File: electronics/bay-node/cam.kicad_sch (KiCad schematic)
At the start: 13 parts, among them J6 CAM, Q4 AO3400A, U12 USBLC6-2SC6, U13 USBLC6-2SC6

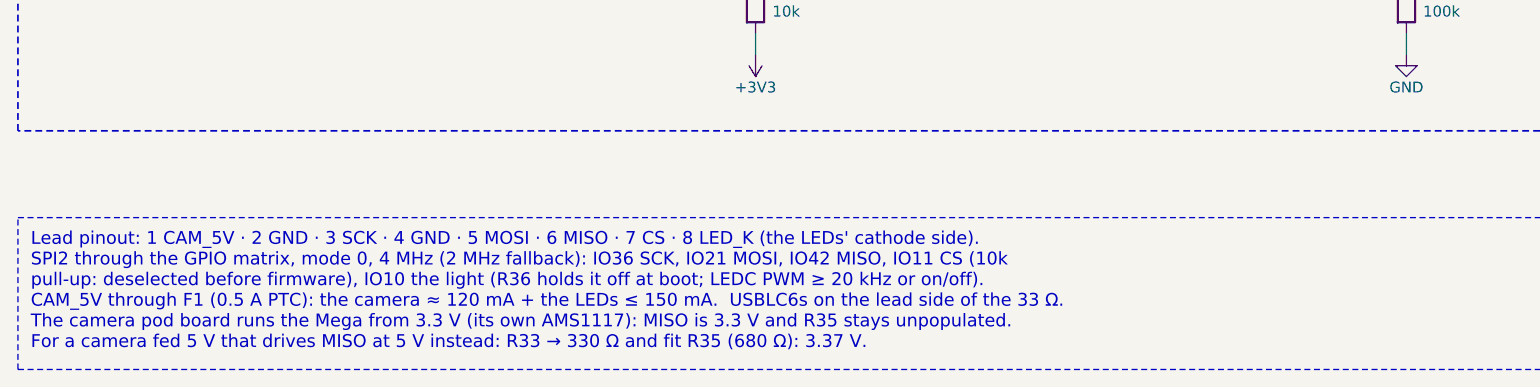
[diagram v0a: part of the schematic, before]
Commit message: PCBA review: hub and node fixes before the order
On main's CH224A hub and the bay node v0.5.

Power hub:
- CPL: the side LEDs (C598310, C4555382) +0.825 mm, their polarity
  proven from JLC's own footprints (and C495809 at 270 deg in the table,
  for the IRF7842 the AP33772S hub had).
- Rows: SHDN pull-downs 10k, so rows stay off without firmware (100k
  gave 1 V at the pin's 10 uA); a B5819W at each row output for the
  cable's kick; the red FAULT LEDs fed from their ROW_EN, so a row that
  is simply off shows no fault.
- In2's VRACK band 8 mm wide; the console's USB pair hand-routed on
  F.Cu over In1 (U5's channels in the pair's order), EN's capacitor at
  the module's pin; reliefs on both pads of C2, C10, R3, C11-C14; notes
  corrected, the outputs sheet on A2.
- The PESD2CAN kept and documented (no stocked CAN TVS stays off at
  29.4 V and clamps under +40 V).

Bay node:
- SW3 placed on its pegs (-0.55 mm, Shouhan's land pattern); 2.2k I2C
  pull-ups; POS_IN 470k; AUX_VREF 1k; 100k on SVC; U9's input on a +5V
  island with three vias, C20 at its pins; C12 relieved; the camera note
  and the catalog's MPN text corrected.

Both re-routed: ERC 0, DRC 0 (the known C8 silkscreen warning), parity
0; CPL audit against JLC's footprints: every part agrees but SW3's pads
(0.13 mm, on purpose).  Bring-up measurements in assembly.md, the
resolution in pcba-review.md.

Co-Authored-By: Claude Opus 5.5 <noreply@anthropic.com>
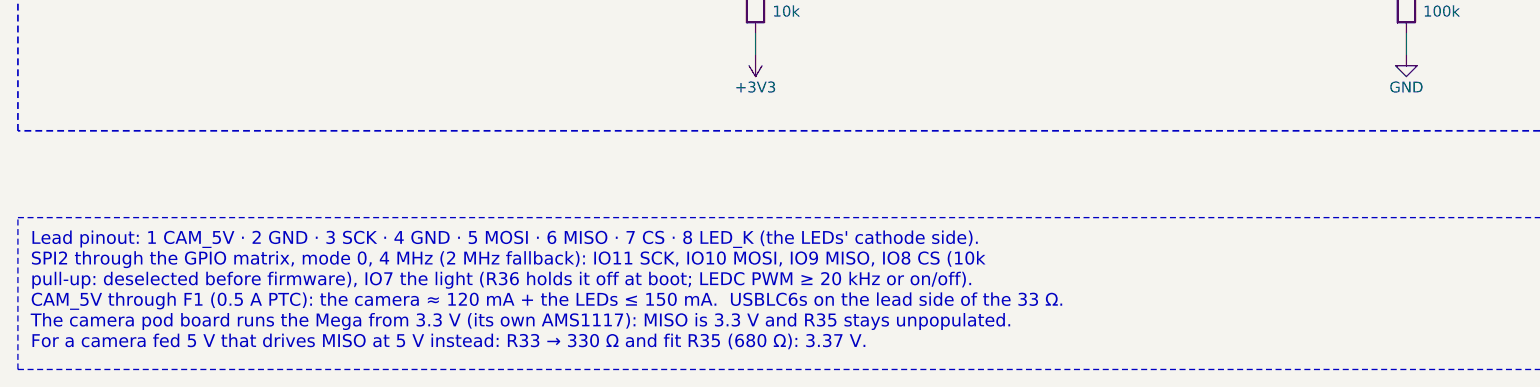
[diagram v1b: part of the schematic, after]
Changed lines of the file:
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@@
 		)
 	)
-	(text_box "Lead pinout: 1 CAM_5V · 2 GND · 3 SCK · 4 GND · 5 MOSI · 6 MISO · 7 CS · 8 LED_K (the LEDs' cathode side).\nSPI2 through the GPIO matrix, mode 0, 4 MHz (2 MHz fallback): IO36 SCK, IO21 MOSI, IO42 MISO, IO11 CS (10k\n  pull-up: deselected before firmware), IO10 the light (R36 holds it off at boot; LEDC PWM ≥ 20 kHz or on/off).\nCAM_5V through F1 (0.5 A PTC): the camera ≈ 120 mA + the LEDs ≤ 150 mA.  USBLC6s on the lead side of the 33 Ω.\nThe camera pod board runs the Mega from 3.3 V (its own AMS1117): MISO is 3.3 V and R35 stays unpopulated.\n  For a camera fed 5 V that drives MISO at 5 V instead: R33 → 330 Ω and fit R35 (680 Ω): 3.37 V."
+	(text_box "Lead pinout: 1 CAM_5V · 2 GND · 3 SCK · 4 GND · 5 MOSI · 6 MISO · 7 CS · 8 LED_K (the LEDs' cathode side).\nSPI2 through the GPIO matrix, mode 0, 4 MHz (2 MHz fallback): IO11 SCK, IO10 MOSI, IO9 MISO, IO8 CS (10k\n  pull-up: deselected before firmware), IO7 the light (R36 holds it off at boot; LEDC PWM ≥ 20 kHz or on/off).\nCAM_5V through F1 (0.5 A PTC): the camera ≈ 120 mA + the LEDs ≤ 150 mA.  USBLC6s on the lead side of the 33 Ω.\nThe camera pod board runs the Mega from 3.3 V (its own AMS1117): MISO is 3.3 V and R35 stays unpopulated.\n  For a camera fed 5 V that drives MISO at 5 V instead: R33 → 330 Ω and fit R35 (680 Ω): 3.37 V."
 		(exclude_from_sim no)
 		(at 15.24 162.56 0)

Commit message: Bay node: AP2114H for the 3.3 V, camera ESD clamped to +3V3
The schematic counter-review's fixes, approved by the user.

- U2: AP2114H-3.3TRG1 (C150716, catalog ldo_1a) instead of the AMS1117-3.3.
  It is specified stable with ceramics (C11, C12); the AMS1117 guarantees it
  only with 22 uF tantalum.  Same SOT-223 "H" pinout (1 GND, 2 and tab VOUT,
  3 VIN), footprint and copper: only the part's properties change.
- U12, U13 (USBLC6 on the camera lead): pin 5 on +3V3 instead of CAM_5V.
  With CAM_5V off (the PTC tripped), the SPI lines would feed the pod through
  the upper diodes, and CAM_5V's clamp sits above the ESP32's 3.6 V.  A
  minimal patch of the routing, no re-route: the CAM_5V stub that only
  reached the two pins goes (10 segments); U12.5 gets a +3V3 feed to a via in
  In2's +3V3 area; U13.5, with no room for its own, joins U12.5 along the
  stub's old east path at 0.25 mm.  The straightening pass ran on +3V3 and
  CAM_5V.
- Stale notes: AUX_VREF goes through R23's 1k, not 33 ohms; the next node's
  pull-down is R29's 470k, not 100k.
- pcbgen.fanout_pads takes `only` (REF.PAD), to fan out a few pads of a
  routed board.

ERC 0, DRC 0, unconnected 0, parity 0, every 3D model found.  The renders,
Gerbers and viewer model are regenerated (the unchanged iso render kept).
The schematic, the BOM and the docs (the node table, the CPL fix table, the
bring-up check, PCBA review N9) follow.  The hub and bom/ are untouched.

Co-Authored-By: Claude Opus 5.5 <noreply@anthropic.com>
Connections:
- net +3V3: now also U12.5 (VBUS), U13.5 (VBUS)
- net CAM_5V: no longer U12.5 (VBUS), U13.5 (VBUS)
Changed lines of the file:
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@@
 		)
 	)
-	(label "CAM_5V"
-		(at 193.04 48.26 90)
-		(fields_autoplaced yes)
-		(effects
-			(font
-				(size 1.27 1.27)
-			)
-			(justify left bottom)
+	(symbol
+		(lib_id "power:+3V3")
+		(at 193.04 48.26 0)
+		(unit 1)
+		(exclude_from_sim no)
+		(in_bom yes)
+		(on_board yes)
+		(dnp no)
+		(fields_autoplaced yes)
+		(property "Reference" "#PWR07006"
+			(at 193.04 48.26 0)
+			(effects
+				(font
+					(size 1.27 1.27)
+				)
+				(hide yes)
+			)
+		)
+		(property "Value" "+3V3"
+			(at 193.04 44.45 0)
+			(effects
+				(font
+					(size 1.27 1.27)
+				)
+			)
+		)
+		(property "Footprint" ""
+			(at 193.04 48.26 0)
+			(effects
+				(font
+					(size 1.27 1.27)
+				)
+				(hide yes)
+			)
+		)
+		(property "Datasheet" ""
+			(at 193.04 48.26 0)
+			(effects
+				(font
+					(size 1.27 1.27)
+				)
+				(hide yes)
+			)
+		)
+		(property "Description" ""
+			(at 193.04 48.26 0)
+			(effects
+				(font
+					(size 1.27 1.27)
+				)
+				(hide yes)
+			)
+		)
+		(pin "1"
+		)
+		(instances
+			(project "bay-node"
+				(path "/76847c0c-2f76-566c-8109-428b2bf58b3f/12078ac0-2350-591d-80c3-fc5243dd3b60"
+					(reference "#PWR07006")
+					(unit 1)
+				)
+			)
 		)
 	)
@@
 		(dnp no)
 		(fields_autoplaced yes)
-		(property "Reference" "#PWR07006"
+		(property "Reference" "#PWR07007"
 			(at 193.04 106.68 0)
 			(effects
@@
 			(project "bay-node"
 				(path "/76847c0c-2f76-566c-8109-428b2bf58b3f/12078ac0-2350-591d-80c3-fc5243dd3b60"
-					(reference "#PWR07006")
+					(reference "#PWR07007")
 					(unit 1)
 				)
@@
 		)
 	)
-	(label "CAM_5V"
-		(at 193.04 88.9 90)
-		(fields_autoplaced yes)
-		(effects
-			(font
-				(size 1.27 1.27)
-			)
-			(justify left bottom)
+	(symbol
+		(lib_id "power:+3V3")
+		(at 193.04 88.9 0)
+		(unit 1)
+		(exclude_from_sim no)
+		(in_bom yes)
+		(on_board yes)
+		(dnp no)
+		(fields_autoplaced yes)
+		(property "Reference" "#PWR07008"
+			(at 193.04 88.9 0)
+			(effects
+				(font
+					(size 1.27 1.27)
+				)
+				(hide yes)
+			)
+		)
+		(property "Value" "+3V3"
+			(at 193.04 85.09 0)
+			(effects
+				(font
+					(size 1.27 1.27)
+				)
+			)
+		)
+		(property "Footprint" ""
+			(at 193.04 88.9 0)
+			(effects
+				(font
+					(size 1.27 1.27)
+				)
+				(hide yes)
+			)
+		)
+		(property "Datasheet" ""
+			(at 193.04 88.9 0)
+			(effects
+				(font
+					(size 1.27 1.27)
+				)
+				(hide yes)
+			)
+		)
+		(property "Description" ""
+			(at 193.04 88.9 0)
+			(effects
+				(font
+					(size 1.27 1.27)
+				)
+				(hide yes)
+			)
+		)
+		(pin "1"
+		)
+		(instances
+			(project "bay-node"
+				(path "/76847c0c-2f76-566c-8109-428b2bf58b3f/12078ac0-2350-591d-80c3-fc5243dd3b60"
+					(reference "#PWR07008")
+					(unit 1)
+				)
+			)
 		)
 	)
@@
 		(dnp no)
 		(fields_autoplaced yes)
-		(property "Reference" "#PWR07007"
+		(property "Reference" "#PWR07009"
 			(at 205.74 139.7 0)
 			(effects
@@
 			(project "bay-node"
 				(path "/76847c0c-2f76-566c-8109-428b2bf58b3f/12078ac0-2350-591d-80c3-fc5243dd3b60"
-					(reference "#PWR07007")
+					(reference "#PWR07009")
 					(unit 1)
 				)
@@
 		(dnp no)
 		(fields_autoplaced yes)
-		(property "Reference" "#PWR07008"
+		(property "Reference" "#PWR07010"
 			(at 177.8 143.51 0)
 			(effects
@@
 			(project "bay-node"
 				(path "/76847c0c-2f76-566c-8109-428b2bf58b3f/12078ac0-2350-591d-80c3-fc5243dd3b60"
-					(reference "#PWR07008")
+					(reference "#PWR07010")
 					(unit 1)
 				)
@@
 		(dnp no)
 		(fields_autoplaced yes)
-		(property "Reference" "#PWR07009"
+		(property "Reference" "#PWR07011"
 			(at 213.36 78.74 0)
 			(effects
@@
 			(project "bay-node"
 				(path "/76847c0c-2f76-566c-8109-428b2bf58b3f/12078ac0-2350-591d-80c3-fc5243dd3b60"
-					(reference "#PWR07009")
+					(reference "#PWR07011")
 					(unit 1)
 				)

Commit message: Schematic review S1, S4, S6: POS_IN 150k, the hub's ON LEDs on 18k, the camera's 0.75 A PTC
The user approved them ("S1 oui / S6 oui / S4 oui").

* S1, bay node: R29 470k -> 150k (C22807, basic).
  - Before its firmware runs, the upstream POS output (a node's IO42, the
    hub's IO10-13) floats. The BAT54S's warm leakage (about 2-3 uA at
    65 C) could then lift POS_IN through 470k to VIL.
  - Driven high through R30 + R28, 150k still gives 2.87 V, above VIH.
  - The design.py notes and bay_node.dtsi follow.
* S4, power hub: R41-R44 (the ON LEDs on the row outputs) 10k -> 18k
  (C25810, already on the board): 1.4 mA and 37 mW at 28 V. The 10k
  ran at 75 % of its 0603 rating at 29.4 V.
* S6, bay node: F1 (CAM_5V) goes from the 0.5 A PTC to SMD1206P075TF
  (RUILON, C20987, new catalog key pptc750): 0.75 A hold, 1.5 A trip,
  the same 1206 footprint. It is extended like C20799, so no fee changes.
  - Arducam gives the Mega 317 mA working: with the LEDs that is
    ~0.42 A on CAM_5V, where the 0.5 A part holds ~0.31 A at 70 C.
  - The camera pod's LDO tab gets the copper its routing leaves: a
    top-side +3V3 pour round the tab and a bottom-side island, joined by
    three vias. U1 drops ~0.5 W at 317 mA. The routing is unchanged.
  - The "~120 mA" notes go to 317 mA (node and pod design.py,
    electronics.md).
  - The bay's worst case follows: <= 2.25 A on +5V, the buck's inductor
    peaking at ~2.65 A (under its 2.9 A minimum limit), 13.5 W from
    VRACK (power-distribution-review.md, the buck notes).

The routed PCBs keep their routing.
- Node and hub: only the changed parts' properties (KiCad's Python, as
  pcbgen sets them).
- Pod: the two new zones and three vias, refilled.
- ERC 0, DRC 0, unconnected 0, parity 0 on all three (run on the Mac:
  zephyrbox didn't answer).
- keep_unchanged kept the node's renders and the hub's Gerbers. The
  hub's bottom render is restored: 9 pixels of via-hole noise, as before.
- The pod's renders, Gerbers and viewer GLB chang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
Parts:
- F1: value 0.5A -> 0.75A; LCSC C20799 -> C20987; MPN SMD1206P050TF -> SMD1206P075TF
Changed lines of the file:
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@@
 			)
 		)
-		(property "Value" "0.5A"
+		(property "Value" "0.75A"
 			(at 50.8 38.176 90)
 			(effects
@@
 			)
 		)
-		(property "Description" "PTC 0.5 A hold, 1206"
+		(property "Description" "PTC 0.75 A hold, 1.5 A trip, 1206"
 			(at 50.8 35.56 0)
 			(effects
@@
 			)
 		)
-		(property "MPN" "SMD1206P050TF"
+		(property "MPN" "SMD1206P075TF"
 			(at 50.8 35.56 0)
 			(effects
@@
 			)
 		)
-		(property "LCSC" "C20799"
+		(property "LCSC" "C20987"
 			(at 50.8 35.56 0)
 			(effects
@@
 		)
 	)
-	(text_box "Lead pinout: 1 CAM_5V · 2 GND · 3 SCK · 4 GND · 5 MOSI · 6 MISO · 7 CS · 8 LED_K (the LEDs' cathode side).\nSPI2 through the GPIO matrix, mode 0, 4 MHz (2 MHz fallback): IO11 SCK, IO10 MOSI, IO9 MISO, IO8 CS (10k\n  pull-up: deselected before firmware), IO7 the light (R36 holds it off at boot; LEDC PWM ≥ 20 kHz or on/off).\nCAM_5V through F1 (0.5 A PTC): the camera ≈ 120 mA + the LEDs ≤ 150 mA.  USBLC6s on the lead side of the 33 Ω.\nThe camera pod board runs the Mega from 3.3 V (its own AMS1117): MISO is 3.3 V and R35 stays unpopulated.\n  For a camera fed 5 V that drives MISO at 5 V instead: R33 → 330 Ω and fit R35 (680 Ω): 3.37 V."
+	(text_box "Lead pinout: 1 CAM_5V · 2 GND · 3 SCK · 4 GND · 5 MOSI · 6 MISO · 7 CS · 8 LED_K (the LEDs' cathode side).\nSPI2 through the GPIO matrix, mode 0, 4 MHz (2 MHz fallback): IO11 SCK, IO10 MOSI, IO9 MISO, IO8 CS (10k\n  pull-up: deselected before firmware), IO7 the light (R36 holds it off at boot; LEDC PWM ≥ 20 kHz or on/off).\nCAM_5V through F1 (0.75 A PTC, 1.5 A trip): the camera ≤ 317 mA (Arducam) + the LEDs ≤ 102 mA.  USBLC6s on the lead side of the 33 Ω.\nThe camera pod board runs the Mega from 3.3 V (its own AMS1117): MISO is 3.3 V and R35 stays unpopulated.\n  For a camera fed 5 V that drives MISO at 5 V instead: R33 → 330 Ω and fit R35 (680 Ω): 3.37 V."
 		(exclude_from_sim no)
 		(at 15.24 162.56 0)

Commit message: Datasheet audit F1-F6: the pod's AP2114H, STB 5.1k, PC_DET hysteresis, the camera ESD's 100 nF, the eFuse step
The user approved the audit's fixes for the node, the hub and the pod
("Go pour 1"); docs/datasheet-audit.md marks F1-F6 applied.

* F1, camera pod: U1 AMS1117-3.3 -> AP2114H-3.3TRG1 (C150716, catalog
  ldo_1a, the node's U2).
  - The AMS1117 is specified stable only with 22 uF tantalum; the
    AP2114H is stable with the ceramic C2.
  - Same SOT-223 pinout, copper (the +3V3 pour and island round the
    tab stay) and 180 deg CPL correction.
  - One more extended type on the pod's Economic order: +$3.09 and
    $0.05 of parts (JLC_SINCE_QUOTE).
* F2, power hub: R214 (TJA1462 STB pull-down) 10k -> 5.1k (C23186,
  already on the board). With IO9 floating, STB's internal pull-up
  (20 kOhm minimum) left it at up to 1.10 V, over VIL 0.99 V.
* F3, bay node: R42 150k from MUX_SEL back to PC_DET, beside U7 (C22807,
  on the board since S1).
  - The laptop's VBUS rises at ~50 us/V through R11/R12, where the
    LVC1G32 wants <= 10 ns/V and warns of oscillation.
  - This gives ~0.14 V of hysteresis.
* F4, bay node: C28 100 nF (C14663) on U12/U13's VBUS pins (+3V3), above
  U12 by its pin 5. Between the two ICs their courtyards leave no room.
* F5, node and hub: firmware.md's first-flash procedure gains the
  irreversible DIS_USB_OTG_DOWNLOAD_MODE eFuse step. In USB-OTG
  download boot the ROM drives IO40 high: the node's DUT_FLT_N, the
  hub's PD_SCL. Nothing is burnt.
* F6, notes, hub:
  - the IMON filter is 0.9 ms, not 47 us: the pin is a current source;
  - the buck stops at ~3.8 V (internal UVLO);
  - SHDN turns on at >= 1 V;
  - the soft start stays under the limit only typically;
  - the CH224A note follows CH224 V2.1: the source PDOs are listed for
    both parts and readable under 100 W, which is still to check with
    ours (review R3); single-byte transfers; no "same die".
* F6, notes, node: TPS2553D; the LDO's 1.94 V x 0.4 A ~ 0.8 W; L1's
  7.5 A guarante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
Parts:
- added C28: 100n, Capacitor_SMD:C_0603_1608Metric, symbol Device:C
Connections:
- net +3V3: now also C28.1
- net GND: now also C28.2

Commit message: Boards: labelled bottom test pads; hub dVdT 100 nF, 50 ms FLT blank
Eve's DFT rule on the four boards this session owns: bare pads on the
bottom, named on B.SilkS, out of the BOM and the CPL (no part, no
assembly fee).  Supply pads 1.5 mm, signal pads 1.0 mm (new catalog
entry "testpad1"), all more than 2 mm from any THT pad or hole
(closest: 4.7 mm, the pod's TP4).  Positions are fixed in design.py,
so they stay put across revisions.

- bay node, 17: TX, RX, 3V3, GND by the module (kept), then EN, IO0,
  FLT (DUT_FLT_N), ALRT (INA_ALERT_N), SDA, SCL and a second GND;
  a supply row along the bottom edge: GND, VIN, 5V, 3V3, DUT 5V,
  CAM 5V
- power hub, 20: TX, RX, 3V3, GND, 5V, VRACK, GND (kept), then EN,
  IO0, the CH224A's PD SDA/SCL, each row's FLT and IMON (A-D) and a
  third GND in the middle
- camera pod, 4: GND, 5V, 3V3 and a second GND at the far end
- DATA port, 2: GND and 5V (VBUS, through a via under its track)

Hub, as the datasheet audit's U1 answer asks (TPS2660 Fig. 55 at
85 C: 8-10 ms at 21 W fails the 47 nF worst start, 33 ms at 14 W
covers 100 nF): C21-C24 dVdT 47 nF -> 100 nF, so a row's soft start
is 16-22 ms and dissipates about 7-9 W typical, 14 W worst, for
19-24 ms; the firmware's HUB_ROW_FLT_BLANK_MS goes 25 -> 50 ms to
cover it (worst case 39 ms).  docs/power.md, the audit row and the
hub notes say so.

Routing fallout: J1's A12/B1 GND now leaves through one drawn 0.5 mm
via so the automatic fan-out can't cut the VRACK pour off A9/B4; the
pod's LDO tab zones are exclusive so tracks no longer split them.

All four rerouted, tidied and checked: ERC 0, DRC 0, unconnected 0,
parity 0.  Gerbers, renders, schematics, viewer GLBs, the JLC
snapshot lines and the rack BOM regenerated.

Co-Authored-By: Claude Opus 5.5 <noreply@anthropic.com>
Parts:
- added TP10: CAM_5V, TestPoint:TestPoint_Pad_D1.5mm, symbol Connector:TestPoint
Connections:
- net CAM_5V: now also TP10.1
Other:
- note added: "CAM_5V test pad (bottom side, in the supply row)"
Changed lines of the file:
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@@
+		)
+	)
+	(symbol
+		(lib_id "Connector:TestPoint")
+		(at 345.44 35.56 90)
+		(unit 1)
+		(exclude_from_sim no)
+		(in_bom no)
+		(on_board yes)
+		(dnp no)
+		(fields_autoplaced yes)
+		(property "Reference" "TP10"
+			(at 338.276 34.29 90)
+			(effects
+				(font
+					(size 1.27 1.27)
+				)
+			)
+		)
+		(property "Value" "CAM_5V"
+			(at 337.226 36.83 90)
+			(effects
+				(font
+					(size 1.27 1.27)
+				)
+			)
+		)
+		(property "Footprint" "TestPoint:TestPoint_Pad_D1.5mm"
+			(at 345.44 35.56 0)
+			(effects
+				(font
+					(size 1.27 1.27)
+				)
+				(hide yes)
+			)
+		)
+		(property "Datasheet" ""
+			(at 345.44 35.56 0)
+			(effects
+				(font
+					(size 1.27 1.27)
+				)
+				(hide yes)
+			)
+		)
+		(property "Description" ""
+			(at 345.44 35.56 0)
+			(effects
+				(font
+					(size 1.27 1.27)
+				)
+				(hide yes)
+			)
+		)
+		(property "MPN" "test pad"
+			(at 345.44 35.56 0)
+			(effects
+				(font
+					(size 1.27 1.27)
+				)
+				(hide yes)
+			)
+		)
+		(property "Manufacturer" "-"
+			(at 345.44 35.56 0)
+			(effects
+				(font
+					(size 1.27 1.27)
+				)
+				(hide yes)
+			)
+		)
+		(pin "1"
+		)
+		(instances
+			(project "bay-node"
+				(path "/76847c0c-2f76-566c-8109-428b2bf58b3f/12078ac0-2350-591d-80c3-fc5243dd3b60"
+					(reference "TP10")
+					(unit 1)
+				)
+			)
+		)
+	)
+	(wire
+		(pts
+			(xy 345.44 35.56)
+			(xy 347.98 35.56)
+		)
+		(stroke
+			(width 0)
+			(type default)
+		)
+	)
+	(label "CAM_5V"
+		(at 347.98 35.56 0)
+		(fields_autoplaced yes)
+		(effects
+			(font
+				(size 1.27 1.27)
+			)
+			(justify left bottom)
 		)
 	)
@@
 		(effects
 			(font
+				(size 1.8 1.8)
+				(bold yes)
+			)
+			(justify left bottom)
+		)
+	)
+	(rectangle
+		(start 314.96 15.24)
+		(end 401.32 55.88)
+		(stroke
+			(width 0.2)
+			(type dash)
+		)
+		(fill
+			(type none)
+		)
+	)
+	(text "CAM_5V test pad (bottom side, in the supply row)"
+		(exclude_from_sim no)
+		(at 316.23 17.78 0)
+		(effects
+			(font

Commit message: Bay node: 15 more labelled bottom test pads (BN-2)
The kicad-happy review's BN-2, against Eve's rule: no pad on the camera
SPI, CAN TXD/RXD, POS_IN/POS_OUT, or the DUT's UART1 and RESET/BOOT, and
all three GND pads in the x 43-46 column.  TP18-TP32 are bare pads on
B.Cu, named on B.SilkS and kept out of the BOM and the CPL.  The
signals are 1.0 mm and each group's GND 1.5 mm:
- the camera SPI by R31-R34, on the lead side of the 33 ohm resistors:
  SCK, MOSI, MISO, CS, GND;
- by U11: CAN TXD, RXD, POS IN, GND;
- by the AUX column: AUX TX, AUX RX, RST, BOOT, POS OUT, GND.

Each pad sits where its net already runs, so no routing moves:
- 8 on a new via drawn on one of the net's F.Cu tracks (the three GNDs
  in the pours);
- 7 on one of the net's B.Cu tracks.
None adds a via on In2's VRACK strip.  All pads are at least 2 mm
from any through-hole pad or hole and 2.6 mm from each other, and no
B.SilkS label overlaps another.  The schematic gets a test pad frame
on each of the Camera, Rack bus and DUT power & AUX sheets.

pcbgen.fanout_pads now leaves alone a pad that holds a drawn via of
its own net (a test pad on its own via).  Fanning it out was
redundant, and in an incremental route the fan-out vias landed on
other nets' tracks.  On the hub, the next regeneration drops TP38's
GND fan-out (1.1 mm and a via); nothing else changes there.

Every track and via is main's, plus one 3 mm CAN_TXD stub that the
router laid over the existing track to reach the new via.  ERC 0,
DRC 0, unconnected 0, parity 0.

Co-Authored-By: Claude Opus 5.5 <noreply@anthropic.com>
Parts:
- added TP18: CAM_SCK_C, TestPoint:TestPoint_Pad_D1.0mm, symbol Connector:TestPoint
- added TP19: CAM_MOSI_C, TestPoint:TestPoint_Pad_D1.0mm, symbol Connector:TestPoint
- added TP20: CAM_MISO_C, TestPoint:TestPoint_Pad_D1.0mm, symbol Connector:TestPoint
- added TP21: CAM_CS_C, TestPoint:TestPoint_Pad_D1.0mm, symbol Connector:TestPoint
- added TP22: GND, TestPoint:TestPoint_Pad_D1.5mm, symbol Connector:TestPoint
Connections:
- net CAM_CS_C: now also TP21.1
- net CAM_MISO_C: now also TP20.1
- net CAM_MOSI_C: now also TP19.1
- net CAM_SCK_C: now also TP18.1
- net GND: now also TP22.1
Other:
- note added: "Test pads, second round (bottom side): the camera SPI and a GND"
